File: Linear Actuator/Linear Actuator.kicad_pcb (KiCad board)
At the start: 2 copper layers, 13 parts, among them J1 Conn_01x02_Pin, J2 Conn_01x02_Pin, U1 NAU7802KGI, U2 ACS772LCB-050B-PFF-T, U3 ACS772LCB-050B-PFF-T

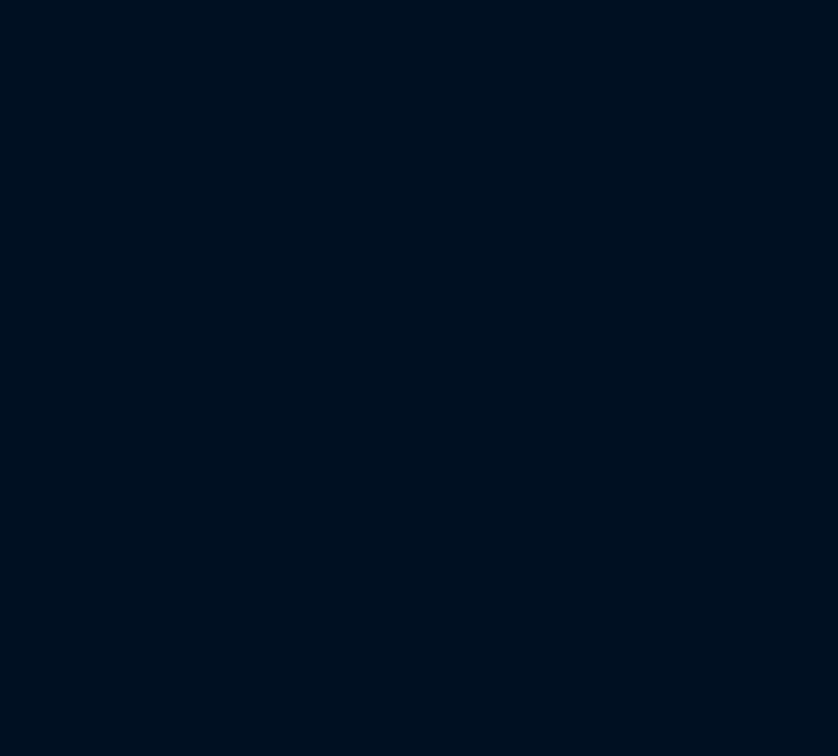
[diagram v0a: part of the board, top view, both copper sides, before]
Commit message: Added breakers, updated footprints
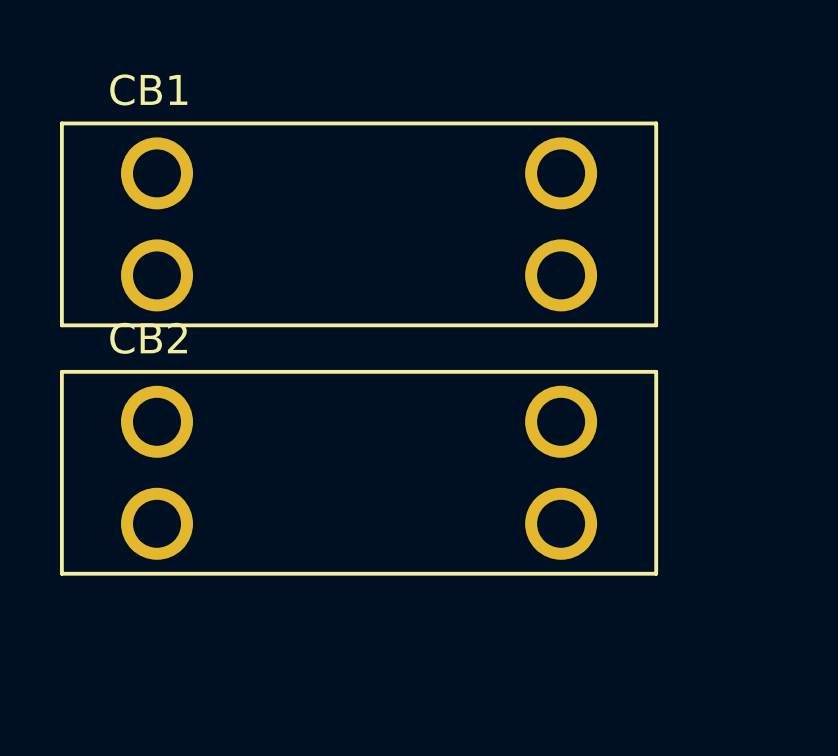
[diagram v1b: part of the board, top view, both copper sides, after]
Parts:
- added CB1: CircuitBreaker_1P_US, linear_actuator_footprints:FUSE_3557-2, F.Cu at (10.2, 3.64)
- added CB2: CircuitBreaker_1P_US, linear_actuator_footprints:FUSE_3557-2, F.Cu at (10.2, 11.9)
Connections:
- U2 pad 4: Net-(J1-Pin_1) -> Net-(CB1-Pad1)
- U3 pad 4: Net-(J2-Pin_1) -> Net-(CB2-Pad1)
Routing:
- net Net-(J2-Pin_1): track 16.1 -> 14.2 mm
- net Net-(CB2-Pad1): track 0.00 -> 1.99 mm
